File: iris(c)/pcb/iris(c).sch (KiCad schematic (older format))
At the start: 66 parts, among them J1 Conn_01x04, SW1 , SW10 , SW11 , SW12 , SW13 config, SW14 , SW15 , SW16 , SW17 , SW18 , SW19 , SW2 , SW20 , SW21 , SW22 , SW23 , SW24 , SW25 , SW26 SW_Push, SW27 , SW28 , SW29 , SW3 , SW30 , SW31 , SW4 , SW5 , SW6 , SW7 , SW8 , SW9 

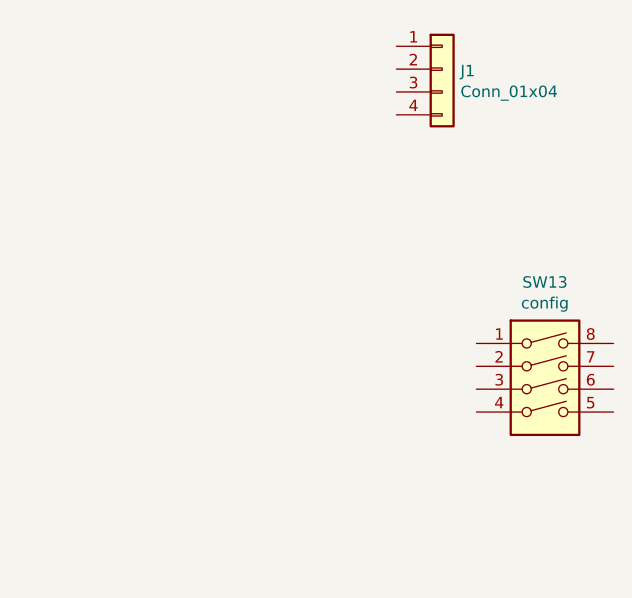
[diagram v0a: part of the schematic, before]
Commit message: add some keyboard
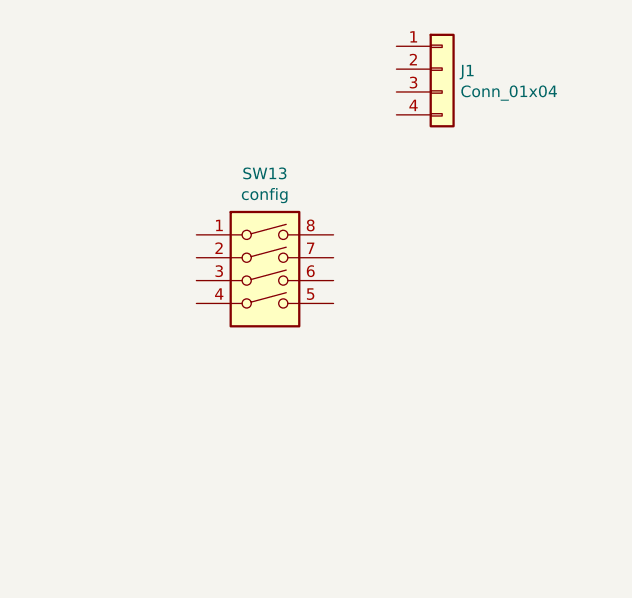
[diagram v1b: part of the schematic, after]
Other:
- moved on the sheet: SW13
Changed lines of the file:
@@
 L Switch:SW_DIP_x04 SW13
 U 1 1 5FE960DA
-P 10500 3275
-F 0 "SW13" H 10500 3742 50  0000 C CNN
-F 1 "config" H 10500 3651 50  0000 C CNN
-F 2 "Button_Switch_SMD:SW_DIP_SPSTx04_Slide_6.7x11.72mm_W6.73mm_P2.54mm_LowProfile_JPin" H 10500 3275 50  0001 C CNN
-F 3 "~" H 10500 3275 50  0001 C CNN
-	1    10500 3275
+P 9275 2800
+F 0 "SW13" H 9275 3267 50  0000 C CNN
+F 1 "config" H 9275 3176 50  0000 C CNN
+F 2 "Button_Switch_SMD:SW_DIP_SPSTx04_Slide_6.7x11.72mm_W6.73mm_P2.54mm_LowProfile_JPin" H 9275 2800 50  0001 C CNN
+F 3 "~" H 9275 2800 50  0001 C CNN
+	1    9275 2800
 	1    0    0    -1
 $EndComp
